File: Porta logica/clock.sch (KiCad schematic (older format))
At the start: 15 parts, among them P4 Ext_Clock, U4 74HC00, U6 LM555N, U7 74HC00

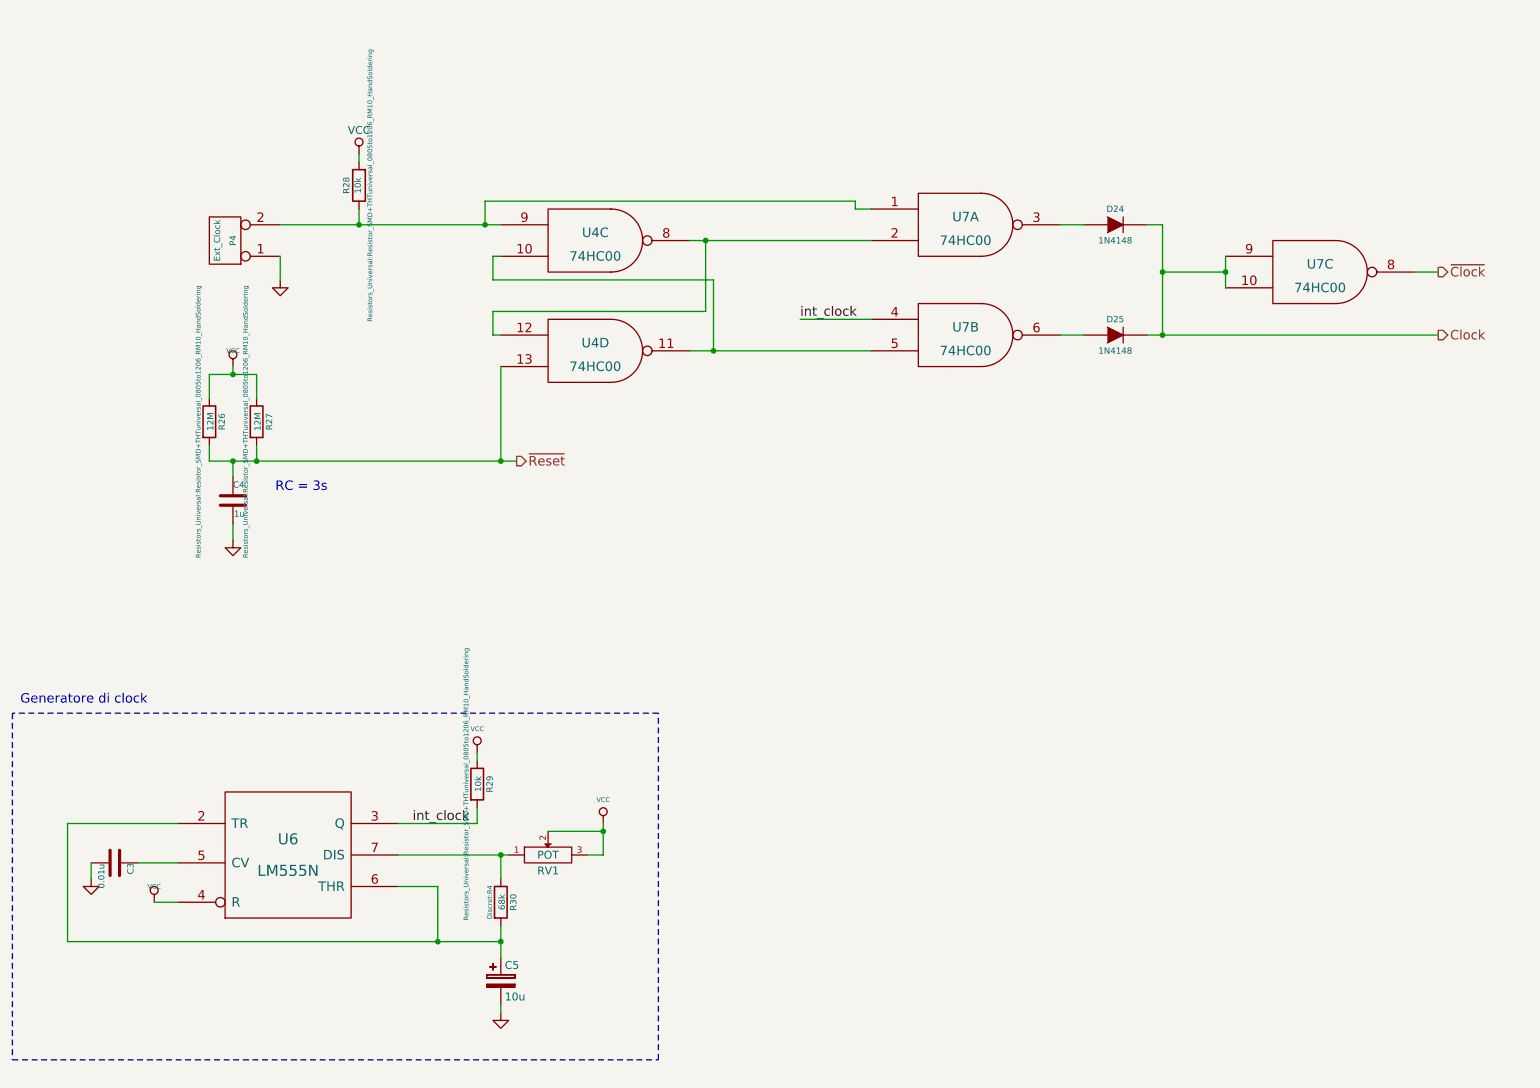
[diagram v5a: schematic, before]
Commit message: Ripulito schematico, migliorato associazioni
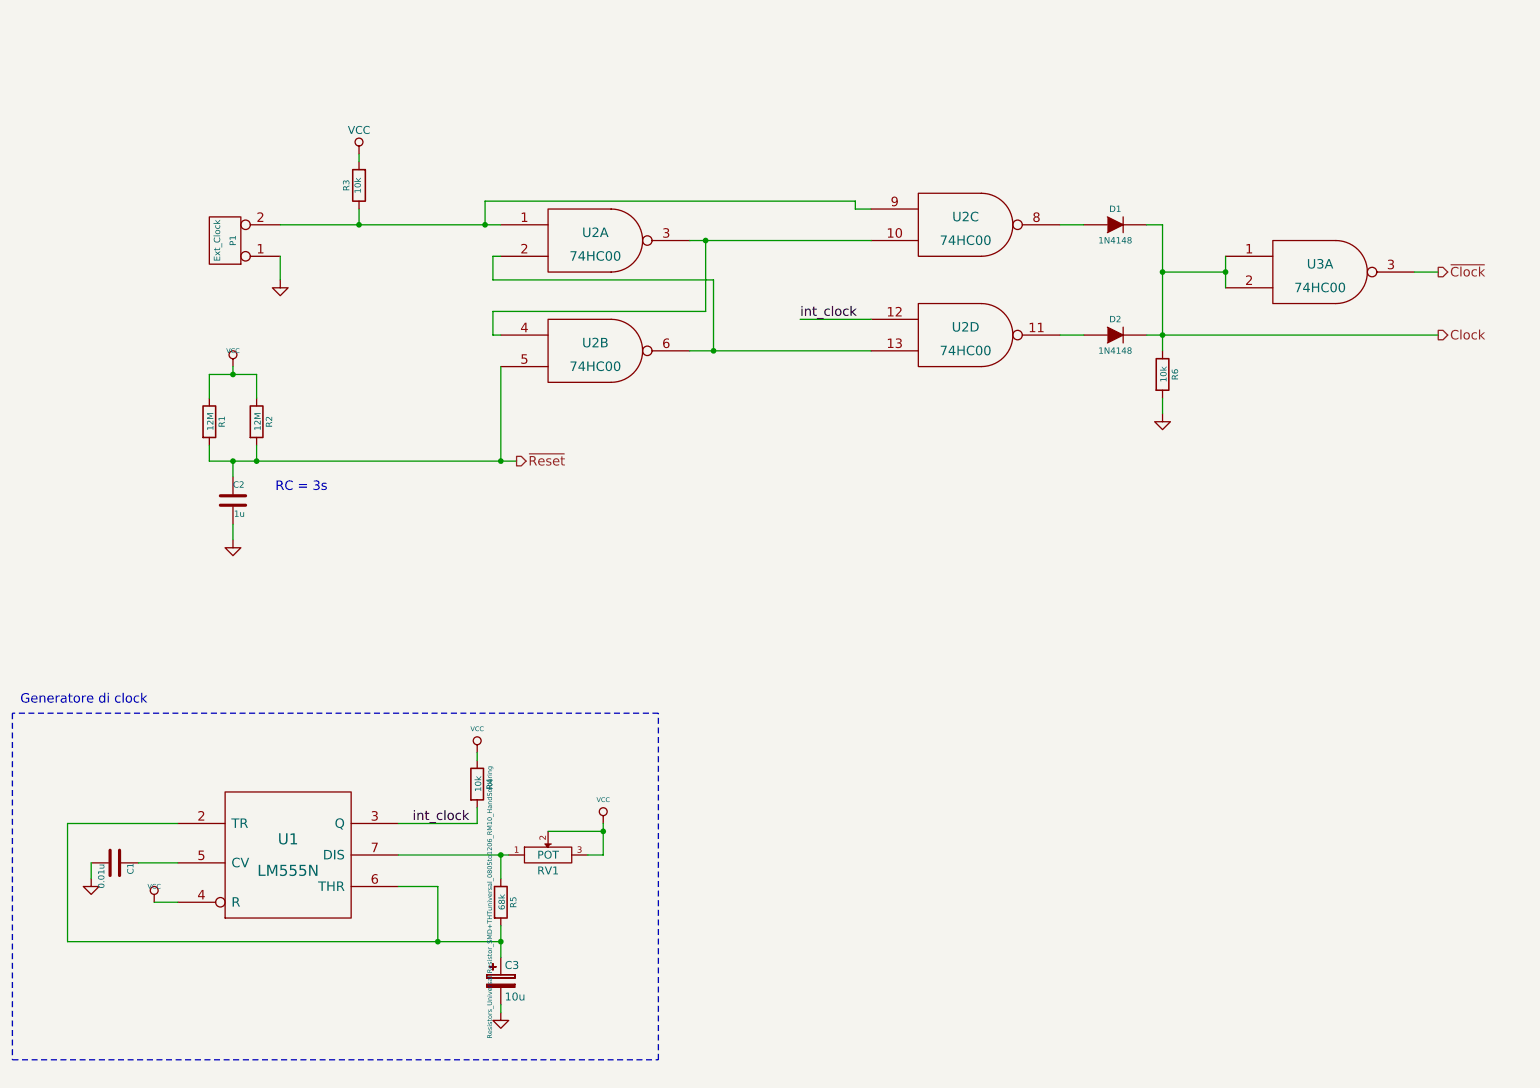
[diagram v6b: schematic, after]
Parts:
- added R6: 10k, Resistors_Universal:Resistor_SMD+THTuniversal_0805to1206_RM10_HandSoldering, symbol R
- D1: renamed from D24; footprint Diodes_ThroughHole:Diode_DO-35_SOD27_Horizontal_RM10 -> LEDs:LED-5MM
- D2: renamed from D25; footprint Diodes_ThroughHole:Diode_DO-35_SOD27_Horizontal_RM10 -> LEDs:LED-5MM
- R5: renamed from R30; footprint Discret:R4 -> Resistors_Universal:Resistor_SMD+THTuniversal_0805to1206_RM10_HandSoldering
- U1: renamed from U6; footprint Housings_SSOP:SSOP-14_5.3x6.2mm_Pitch0.65mm -> Housings_SOIC:SOIC-16_7.5x10.3mm_Pitch1.27mm
- U2: renamed from U7; footprint Housings_SOIC:SOIC-8_3.9x4.9mm_Pitch1.27mm -> Housings_SOIC:SOIC-16_7.5x10.3mm_Pitch1.27mm
- U3: renamed from U7; footprint Housings_SOIC:SOIC-8_3.9x4.9mm_Pitch1.27mm -> Housings_SOIC:SOIC-14_3.9x8.7mm_Pitch1.27mm
- renumbered C3 to C1, C4 to C2, C5 to C3, P4 to P1, R26 to R1, R27 to R2, R28 to R3, R29 to R4, U4 to U2
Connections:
- net Clock: now also U3.1, U3.2, R6.1; no longer U3.10, U3.9
- net GND: now also R6.2
- net int_clock: now also U2.12; no longer U2.4
- net ~Clock: now also U3.3; no longer U3.8
- net ~Reset: now also U2.5; no longer U2.13
- net at P1.2 (PM), R3.1: now also U2.1, U2.9; no longer U2.1, U2.9
- net at D1.1 (A): now also U2.8; no longer U2.3
- net at D2.1 (A): now also U2.11; no longer U2.6
- new net: U2.13, U2.2, U2.6
- new net: U2.10, U2.3, U2.4
